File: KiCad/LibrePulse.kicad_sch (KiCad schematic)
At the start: 120 parts, among them IC1 TPS62840YBGR, IC2 BQ21088YBGR, IC3 AS6221, IC4 BME690, IC5 ICU-10201, IC6 KLMCG4JETD-B041, J1 Micro_SD_Card, M1 VLV041235L, U1 AS7058, U10 TPS63020, U11 ESP32-P4NRW32, U12 BMI270, U13 PCAL6416AHF, U14 BMM350, U15 DRV2605LDGS, U16 MAX98357A, U17 W25Q128JVE, U18 LM3643YFFR, U19 ESP32-C3, U2 ET020AM03-HT, U20 ASGPDF254_A, U3 RV-3028-C8-32.768KHZ-1PPM-TA-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, U4 MS5837-xxBA, U5 BQ27427YZFR, U6 BQ51013CQWRHLRQ1, U7 LTR-390UV-01, U8 TCA9548AMRGER, U9 760308101214

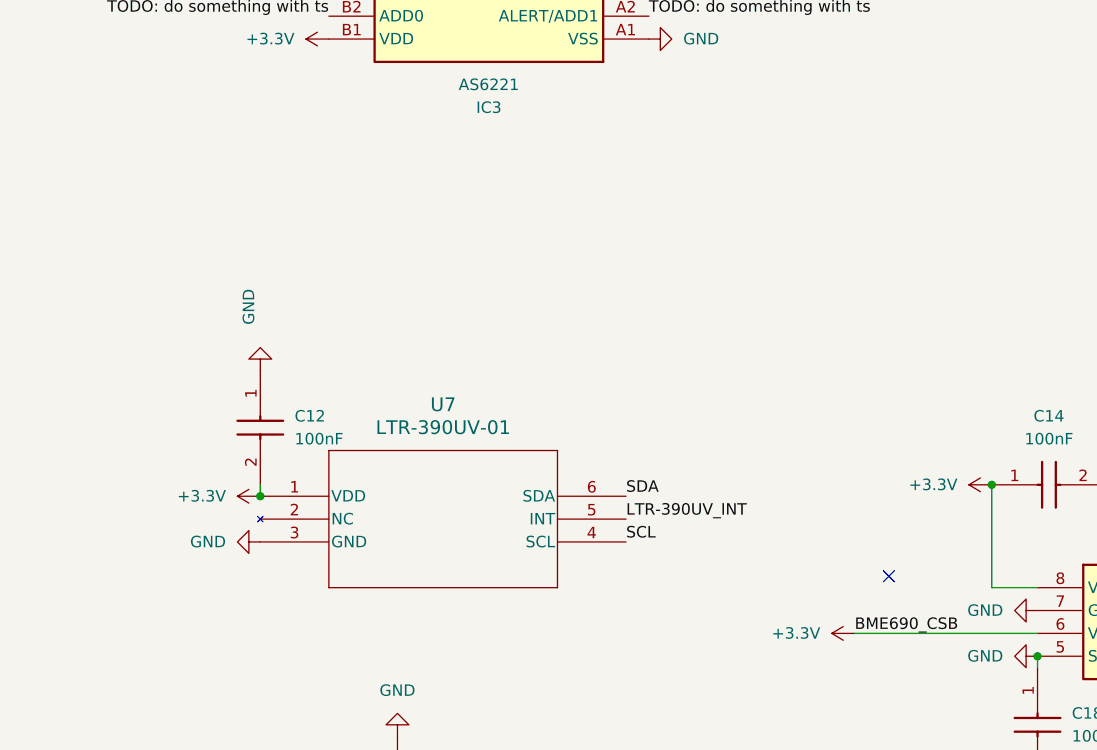
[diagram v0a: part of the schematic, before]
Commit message: Replace obsolete LTR390-UV with TI OPT3007 and ams AS7331
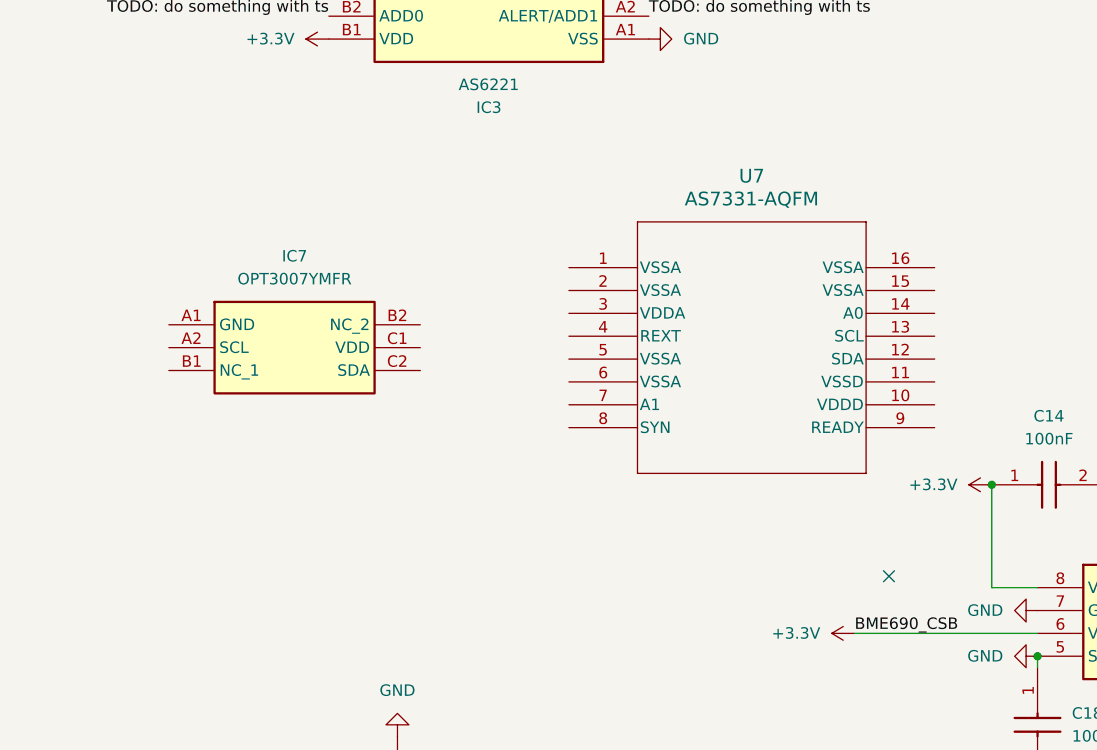
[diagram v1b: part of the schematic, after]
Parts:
- removed C12: 100nF, Footprints:GRM033D70J224ME01D, symbol Symbols:GRM033Z71C104KE14J
- removed U7: LTR-390UV-01, Footprints:LTR-390UV, symbol 2026-08-10_15-14-30:LTR-390UV-01
- added IC7: OPT3007YMFR, BGA6C35P2X3_86X95X23, symbol Symbols:OPT3007YMFR
- added U7: AS7331-AQFM, OLGA16_AS7331_OSM, symbol Symbols:AS7331-AQFM

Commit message: finish 1.2V
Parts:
- removed C19, C20: 10uF, Footprints:GRM21BR60J226ME39L, symbol Symbols:GRM21BZ71E106KE15L
- removed C21, C22: 22uF, Footprints:GRM31x, symbol Symbols:GRM31CZ71C226ME15L
- removed C28: 100nF, Footprints:GRM033D70J224ME01D, symbol Symbols:GRM033Z71C104KE14J
- removed IC1: TPS62840YBGR, Footprints:BGA6C40P3X2_149X102X60, symbol Symbols:TPS62840YBGR
- removed L1: 2.2uH, Footprints:744777002, symbol Symbols:744777002
- removed U10: TPS63020, Footprints:TPS63020, symbol TPS63020:TPS63020
- added C12: 10uF, GRM21BR60J226ME39L, symbol Symbols:GRM21BZ71E106KE15L
- added C68: 4.7uF, GRM21BR60J226ME39L, symbol Symbols:GRM21BZ71E475KE15L
- added IC1: TPS62841YBGR, BGA6C40P2X3_97X147X50, symbol Symbols:TPS62841YBGR
- added L4: 2.2uH, Footprints:744777002, symbol Symbols:744777002
- added R16: 16k, ERJU01_(0201), symbol Symbols:ERJU01F1602C
- U4: value MS5837-xxBA -> MS5837-30BA
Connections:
- net +1.2V: now also C12.1, IC1.A2 (VOS), L4.2
- net GND: now also C5.2, C12.2, C68.2, IC1.A1 (GND), R16.2; no longer C5.1
- net U6_4: now also C5.1; no longer C5.2
- net SYS renamed 1.2V
- net 1.2V: now also C68.1, IC1.B1 (VIN)
- new net: IC1.B2 (SW), L4.1
- new net: IC1.C2 (VSET), R16.1
- new net IC1_C1: IC1.C1 (EN)
- no-connect marks 21 -> 20
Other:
- note added: "TPS62841YBGR"
- note removed: "TPS62840YBGR"
- moved on the sheet: U1

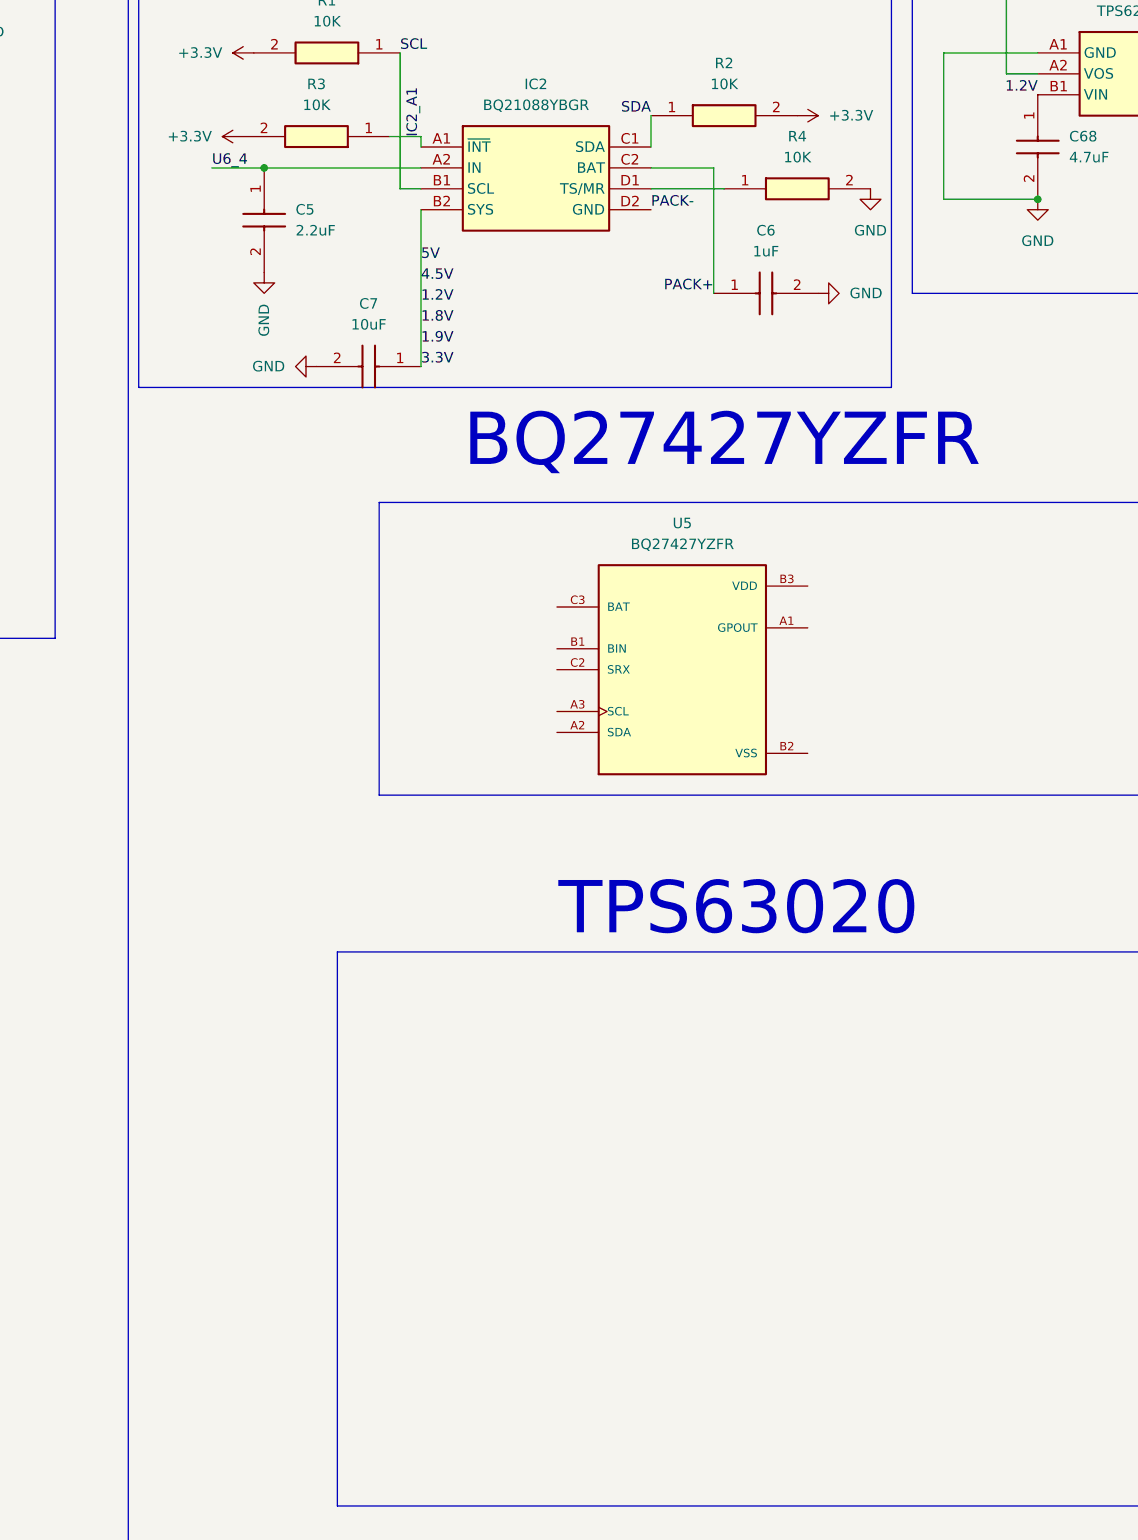
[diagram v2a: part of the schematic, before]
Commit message: begin 5V, fixup 1.2V
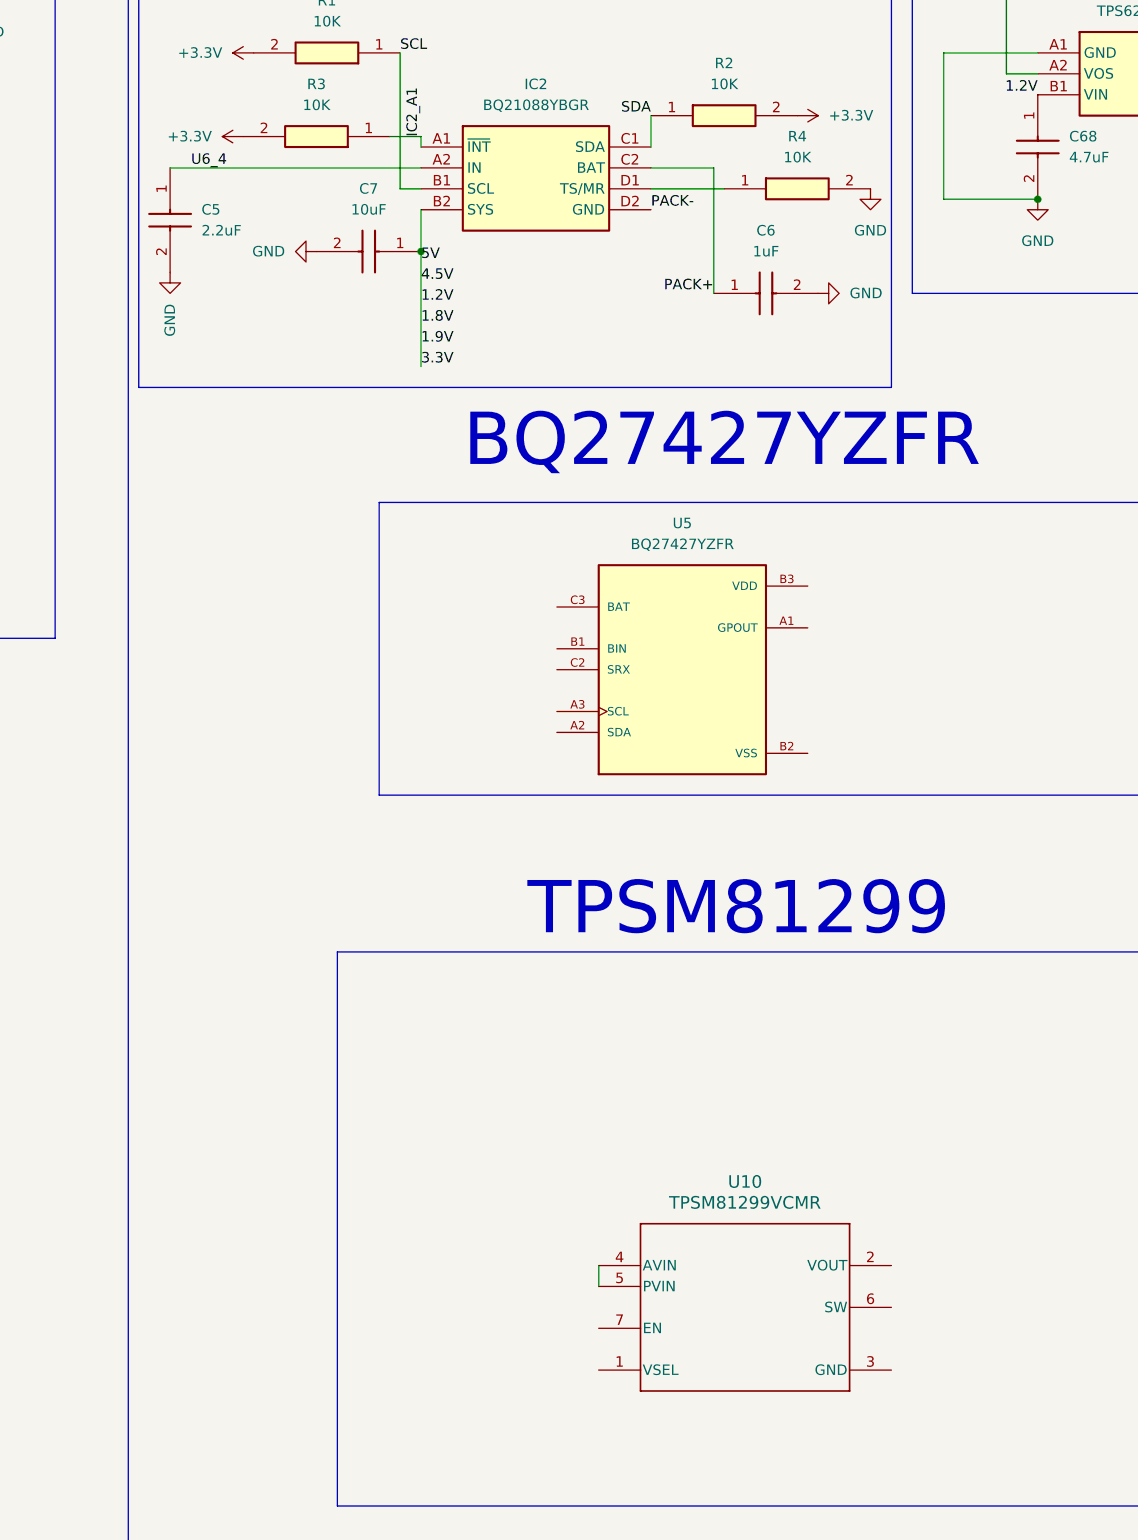
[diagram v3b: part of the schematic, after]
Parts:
- added U10: TPSM81299VCMR, VCM0007A-MFG, symbol Symbols:TPSM81299VCMR
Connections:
- new net: U10.4 (AVIN), U10.5 (PVIN)
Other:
- note added: "TPSM81299"
- note removed: "TPS63020"
- moved on the sheet: C5
